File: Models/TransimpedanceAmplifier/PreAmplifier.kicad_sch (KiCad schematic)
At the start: 6 parts, among them U5 AD8615AUJZ-R2

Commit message: Save progress
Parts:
- added C1, C2: 470 uF, symbol Device:C_Polarized_US
- added C3, C4: 470 nF, symbol Device:C
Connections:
- net -1.5V: now also C2.2, C4.2
- net 2.5V: now also C1.1, C3.1
- net GND: now also U5.3 (IN+), C1.2, C2.1, C3.2, C4.1
- net Output: now reaches U5.1 (OUT)
- net Input: now reaches U5.4 (IN-)
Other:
- note added: "Local decoupling network"
- note added: "Voltage divider"
- moved on the sheet: D1, R3, R4, R5, RV4, U5

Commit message: Save progress
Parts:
- RV4: value 1k -> 1k, 10%
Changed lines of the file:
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@@
 	(rectangle
 		(start 205.74 33.02)
-		(end 241.3 132.08)
+		(end 243.84 132.08)
 		(stroke
 			(width 0)
@@
 			)
 		)
-		(property "Value" "1k"
+		(property "Value" "1k, 10%"
 			(at 233.68 53.3399 0)
 			(effects

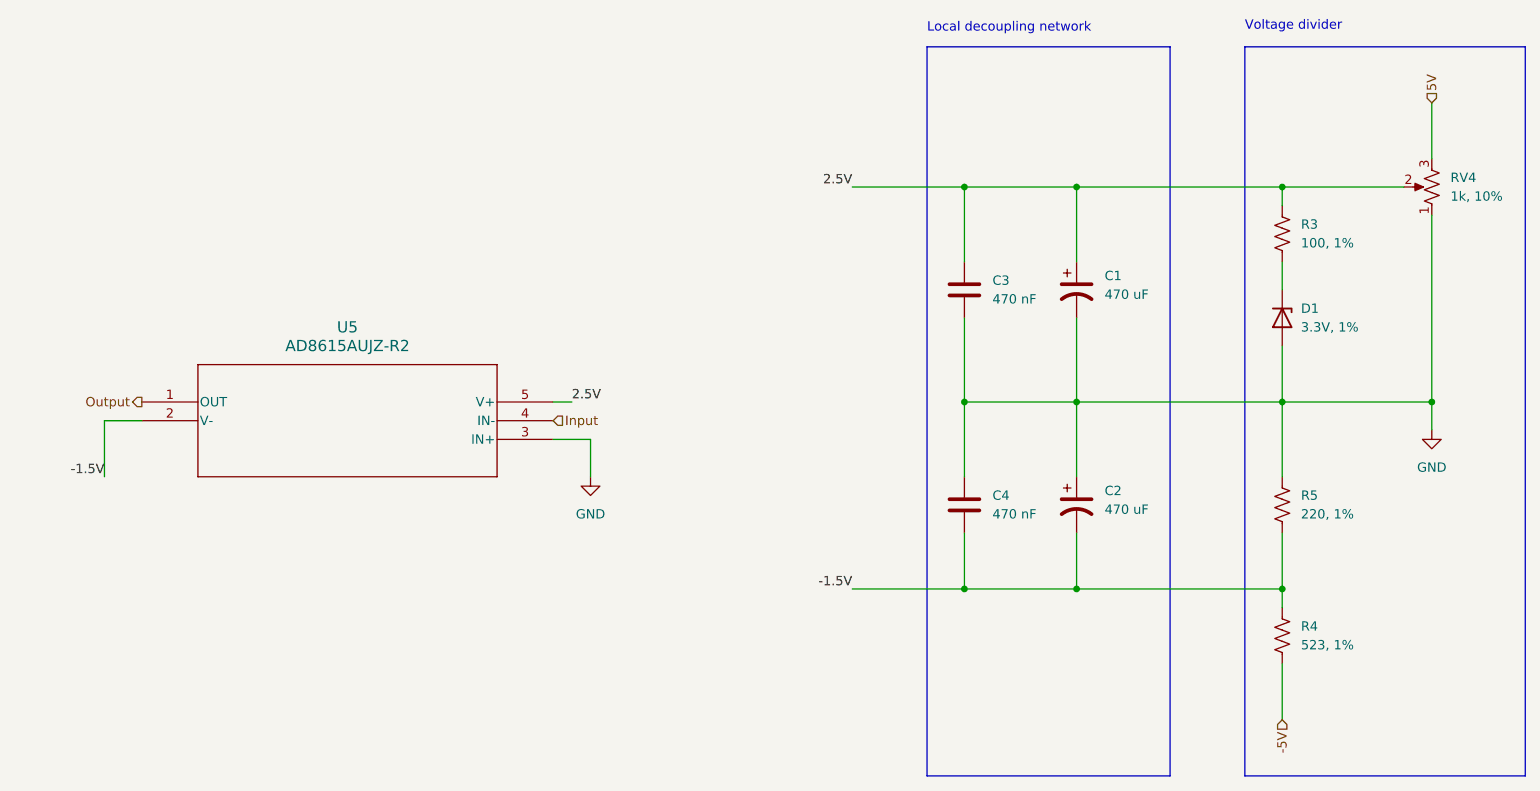
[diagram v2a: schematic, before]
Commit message: Added purchase links for all current capacitors, with dimensional tolerances matching the footprint
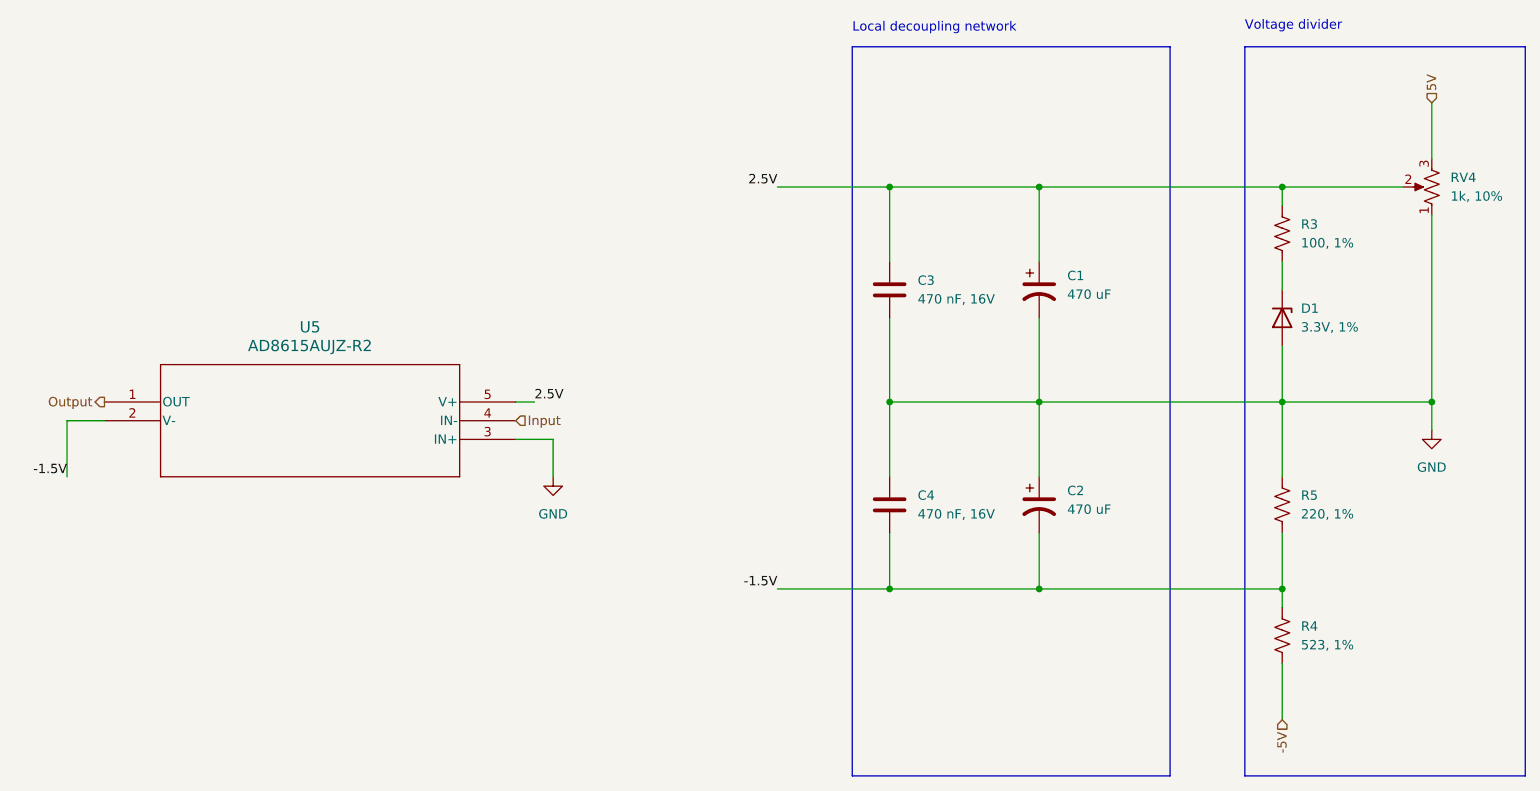
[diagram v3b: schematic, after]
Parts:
- C3, C4: value 470 nF -> 470 nF, 16V; Purchase Link (none) -> https://www.digikey.com/en/products/detail/murata-electroni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
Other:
- moved on the sheet: C1, C2, C3, C4, U5

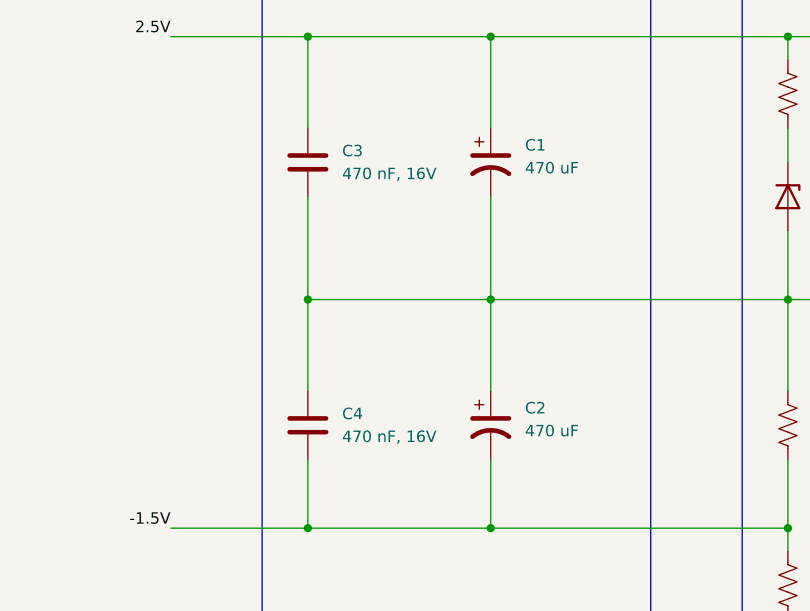
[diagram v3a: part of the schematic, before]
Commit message: Switched to a better capacitor product
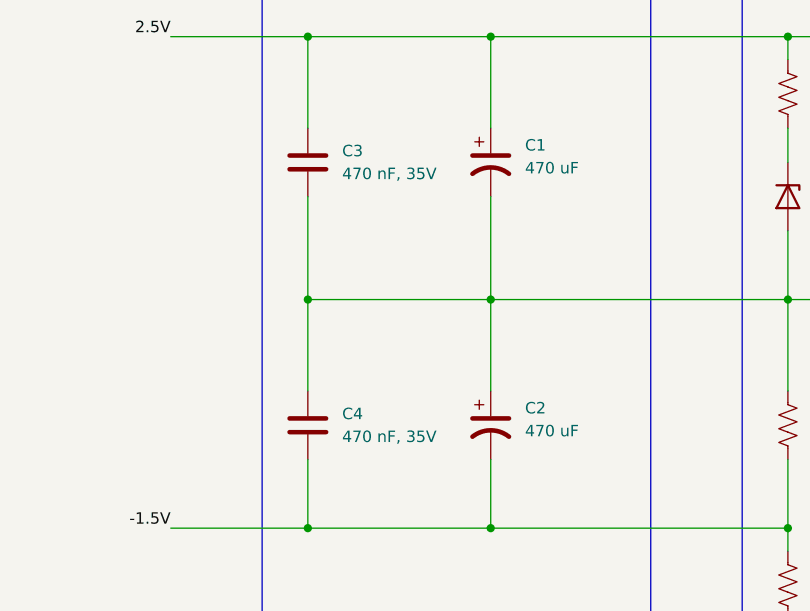
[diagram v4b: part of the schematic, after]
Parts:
- C3, C4: value 470 nF, 16V -> 470 nF, 35V; Purchase Link https://www.digikey.com/en/products/detail/murata-electronics/GRM188R71C474KA88D/702559 -> https://www.digikey.com/en/products/detail/murata-electronics/GRM188R7YA474KE05D/10701970
- RV4: Purchase Link (none) -> https://www.digikey.com/en/products/detail/bourns-inc/3269W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
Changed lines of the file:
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@@
 			)
 		)
-		(property "Value" "470 nF, 16V"
+		(property "Value" "470 nF, 35V"
 			(at 161.29 96.5199 0)
 			(effects
@@
 			)
 		)
-		(property "Purchase Link" "https://www.digikey.com/en/products/detail/murata-electronics/GRM188R71C474KA88D/702559"
+		(property "Purchase Link" "https://www.digikey.com/en/products/detail/murata-electronics/GRM188R7YA474KE05D/10701970"
 			(at 157.48 95.25 0)
 			(effects
@@
 			)
 		)
+		(property "Purchase Link" "https://www.digikey.com/en/products/detail/bourns-inc/3269W-1-102GLF/2535565"
+			(at 231.14 52.07 0)
+			(effects
+				(font
+					(size 1.27 1.27)
+				)
+				(hide yes)
+			)
+		)
 		(pin "2"
 		)
@@
 			)
 		)
-		(property "Value" "470 nF, 16V"
+		(property "Value" "470 nF, 35V"
 			(at 161.29 67.3099 0)
 			(effects
@@
 			)
 		)
-		(property "Purchase Link" "https://www.digikey.com/en/products/detail/murata-electronics/GRM188R71C474KA88D/702559"
+		(property "Purchase Link" "https://www.digikey.com/en/products/detail/murata-electronics/GRM188R7YA474KE05D/10701970"
 			(at 157.48 66.04 0)
 			(effects

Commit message: Got the purchase links for the remaining discrete devices in this task
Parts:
- D1: Purchase Link (none) -> https://www.digikey.com/en/products/detail/diodes-incorpora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
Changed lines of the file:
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@@
+			)
+		)
+		(property "Purchase Link" "https://www.digikey.com/en/products/detail/diodes-incorporated/LM4040D33FTA/10295608"
+			(at 210.82 69.85 0)
+			(effects
+				(font
+					(size 1.27 1.27)
+				)
+				(hide yes)
 			)
 		)

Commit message: All suppliers are out of stock of LM7915L in the simple TO-92-3 package. Resolve this by first tabulating the maximum possible current on each regulator.
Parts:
- U5: Purchase Link (none) -> https://www.digikey.com/en/products/detail/analog-devices-i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
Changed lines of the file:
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@@
+			)
+		)
+		(property "Purchase Link" "https://www.digikey.com/en/products/detail/analog-devices-inc/AD8615AUJZ-REEL7/951437"
+			(at 50.8 81.28 0)
+			(effects
+				(font
+					(size 1.27 1.27)
+				)
+				(hide yes)
 			)
 		)

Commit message: Overhauled the purchase links for regulators and trimpots
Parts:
- RV4: Purchase Link https://www.digikey.com/en/products/detail/bourns-inc/3269W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 -> https://www.digikey.com/en/products/detail/bourns-inc/3296Y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
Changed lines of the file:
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@@
 			)
 		)
-		(property "Purchase Link" "https://www.digikey.com/en/products/detail/bourns-inc/3269W-1-102GLF/2535565"
+		(property "Purchase Link" "https://www.digikey.com/en/products/detail/bourns-inc/3296Y-1-102LF/1088084"
 			(at 231.14 52.07 0)
 			(effects

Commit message: Refactoring in progress
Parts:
- removed C1, C2: 470 uF, symbol Device:C_Polarized_US
- added C1: 1 uF, 0603, symbol Device:C
- added C2: 10 uF, 0805, symbol Device:C
- C3: value 470 nF, 35V -> 1 uF, 0603; Purchase Link https://www.digikey.com/en/products/detail/murata-electroni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 -> (none)
- C4: value 470 nF, 35V -> 10 uF, 0805; Purchase Link https://www.digikey.com/en/products/detail/murata-electroni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 -> (none)
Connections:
- net -1.5V: now also C3.2
- net 2.5V: now also C1.1, C2.1; no longer C3.1
- net GND: now also C3.1, C1.2, C2.2; no longer C3.2
